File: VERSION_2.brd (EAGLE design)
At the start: 73.6 x 41.6 mm, 57 parts, among them J1 MICRO-SD_CARD_SOCKET

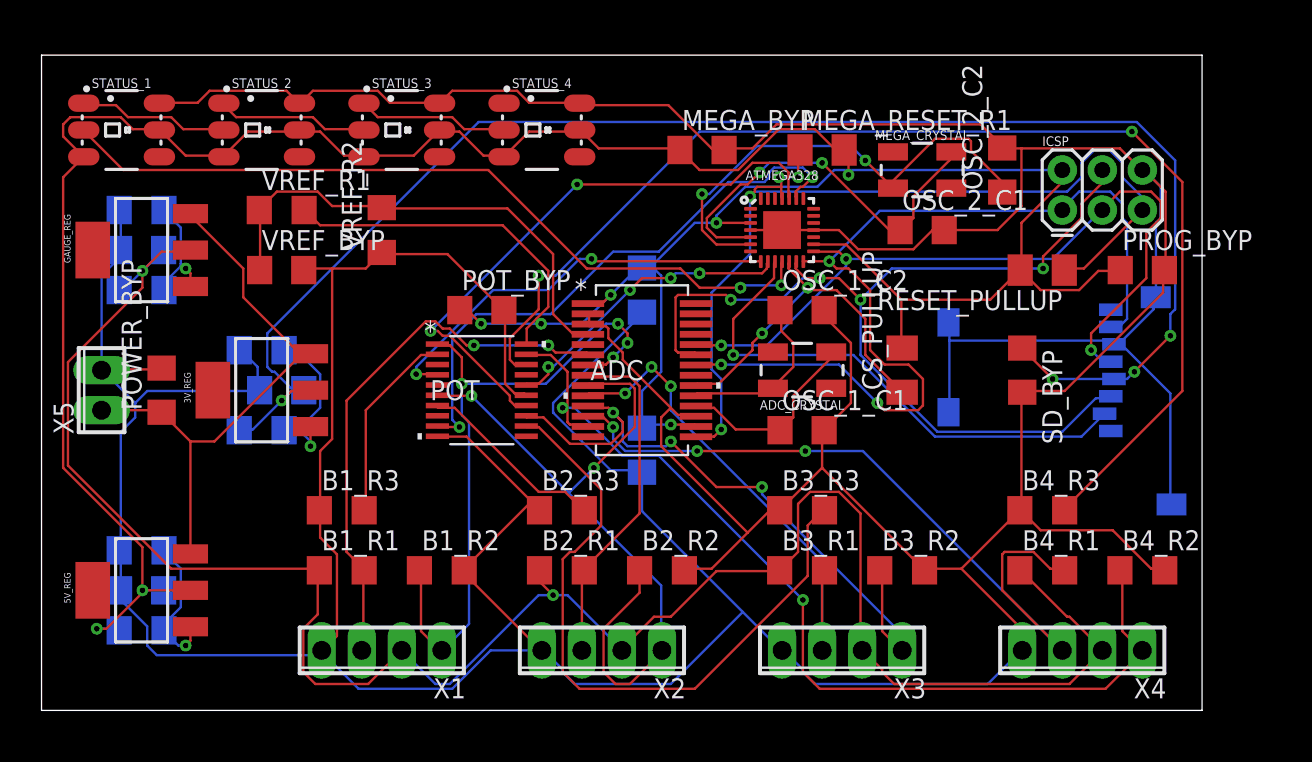
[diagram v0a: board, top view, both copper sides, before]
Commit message: Size and DRC Optimizations
Final size: 1.5"x2.5". Might be a little tricky to solder now, but oh well
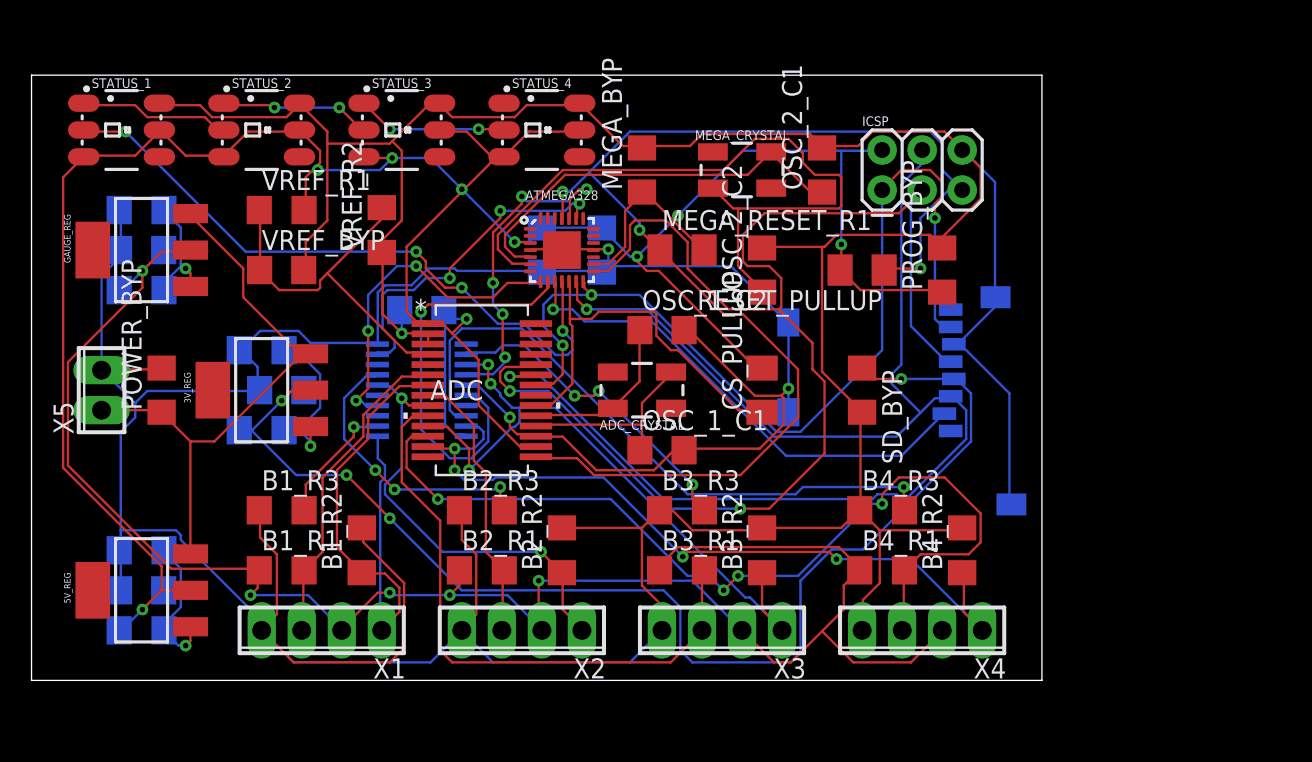
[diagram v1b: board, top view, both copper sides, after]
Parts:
- moved OSC_2_C2 16.5 mm to (45.7, 27.9)
- moved ATMEGA328 14.0 mm to (33.0, 29.2)
- moved ADC_BYP_A 13.0 mm to (35.6, 29.2)
- moved PROG_BYP 12.7 mm to (57.1, 27.9), turned to 90 degrees
- moved B4_R2 11.5 mm to (58.4, 10.2), turned to 90 degrees
- moved ICSP 11.5 mm to (53.3, 33.0)
- moved MEGA_CRYSTAL 11.4 mm to (44.5, 34.3)
- moved RESET_PULLUP 11.4 mm to (52.1, 27.9)
- moved MEGA_RESET_R1 10.9 mm to (40.6, 29.2)
- moved X4 10.2 mm to (55.9, 5.08)
- moved ADC 10.2 mm to (27.9, 20.3)
- moved ADC_CRYSTAL 10.2 mm to (38.1, 20.3)
- moved SD_BYP 10.2 mm to (52.1, 20.3)
- moved B4_R1 10.2 mm to (53.3, 8.89)
- moved B4_R3 10.2 mm to (53.3, 12.7)
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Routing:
- net GND: track 443.6 -> 396.3 mm, vias 0 -> 4
- net SCK: track 49.2 -> 87.7 mm, vias 3 -> 2
- net POT4: track 77.1 -> 40.7 mm, vias 2 -> 1
- net +5V: track 219.9 -> 192.5 mm, vias 8 -> 9
- net MOSI: track 62.7 -> 86.6 mm, vias 4 -> 2
- net POT3: track 42.8 -> 20.5 mm, vias 0 -> 3
- net RESET: track 60.4 -> 80.4 mm, vias 4 -> 3
- net B2_-: track 47.4 -> 27.8 mm
- net +3V: track 99.1 -> 80.6 mm
- net +V: track 130.8 -> 114.5 mm, vias 2 -> 5
- net SCL: track 37.2 -> 21.6 mm, vias 2 -> 5
- net SDA: track 36.9 -> 21.5 mm, vias 2 -> 3
- net N$5: track 31.1 -> 45.6 mm, vias 2 -> 0
- net B1_+: track 34.7 -> 20.4 mm, vias 2 -> 0
- net B4_-: track 61.8 -> 49.3 mm, vias 2 -> 4
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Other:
- board size 73.6 x 41.6 mm -> 64.1 x 38.4 mm

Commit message: Optimized size and solderability
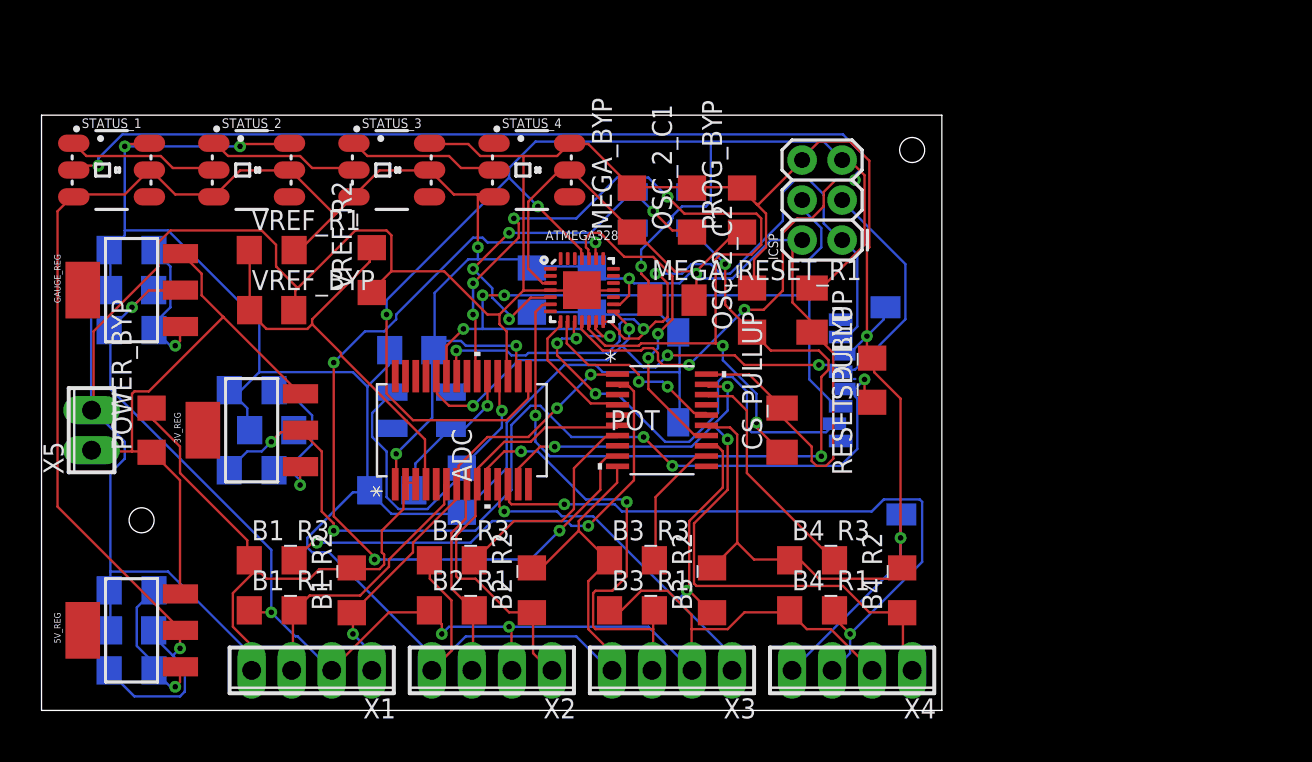
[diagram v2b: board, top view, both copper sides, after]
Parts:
- moved OSC_1_C2 19.9 mm to (22.2, 14.0), flipped to the bottom
- moved POT 15.4 mm to (39.4, 18.4), flipped to the top, turned to 0 degrees
- moved ADC_CRYSTAL 14.0 mm to (24.1, 19.1), flipped to the bottom
- moved PROG_BYP 13.3 mm to (44.5, 31.8)
- moved OSC_1_C1 13.0 mm to (26.7, 14.0), flipped to the bottom, turned to 270 degrees
- moved OSC_2_C1 8.64 mm to (41.3, 31.8)
- moved J1 7.01 mm to (40.0, 26.0)
- moved MEGA_CRYSTAL 5.68 mm to (39.4, 31.8), flipped to the bottom
- moved B4_R3 5.46 mm to (48.9, 9.53)
- moved B4_R1 5.12 mm to (48.9, 6.35)
- moved X4 5.12 mm to (51.4, 2.54)
- moved B4_R2 4.58 mm to (54.6, 7.62)
- moved B3_R3 4.49 mm to (37.5, 9.53)
- moved ICSP 4.07 mm to (50.8, 29.8), turned to 90 degrees
- moved B3_R1 4.07 mm to (37.5, 6.35)
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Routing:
- net SCK: track 87.7 -> 47.5 mm, vias 2 -> 4
- net STATUS_IN: track 41.9 -> 80.4 mm
- net MOSI: track 86.6 -> 52.3 mm, vias 2 -> 4
- net SDA: track 21.5 -> 53.9 mm, vias 3 -> 4
- net CS: track 25.3 -> 57.5 mm, vias 0 -> 6
- net POT4: track 40.7 -> 14.8 mm, vias 1 -> 0
- net +V: track 114.5 -> 89.6 mm, vias 5 -> 4
- net POT1: track 8.10 -> 30.8 mm, vias 1 -> 2
- net +3V: track 80.6 -> 62.2 mm, vias 4 -> 5
- net B4_+: track 58.3 -> 43.0 mm, vias 4 -> 2
- net POT_A1: track 25.9 -> 12.5 mm, vias 1 -> 2
- net POT_A0: track 21.5 -> 8.48 mm, vias 3 -> 0
- net POT3: track 20.5 -> 8.36 mm, vias 3 -> 0
- net MISO: track 60.4 -> 49.8 mm
- net B3_+: track 38.8 -> 28.8 mm, vias 0 -> 2
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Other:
- board size 64.1 x 38.4 mm -> 57.1 x 37.8 mm
